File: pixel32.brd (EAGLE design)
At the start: 50 x 40 mm, 111 parts, among them CON1 DS1066-07M-SIDE, CON2 DS1066-07M-SIDE, CON3 PINHEAD_1X02-2.54, CON4 PINHEAD_1X01-2.54, CON5 PINHEAD_1X01-2.54, CON6 PINHEAD_1X01-2.54, CON7 PINHEAD_1X01-2.54, IC1 STM32F030K6TX-LQFP32(7X7), IC101 IRS44273L, IC201 IRS44273L, IC3 ST3485SOIC8, IC301 IRS44273L, IC6 MC74VHC1GT125, IC7 MC74VHC1GT125, IC8 LM317

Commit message: PCB Finalization #2
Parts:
- added FRAME1, FRAME101, FRAME201, FRAME301: RTU_A4, frames:A4L-LOC
- added FRAME2: RTU_A3, frames:A3L-LOC
- moved R10 4.16 mm to (-5.22, -1.82), turned to 45 degrees
- moved R13 3.03 mm to (-3.95, 0.70), turned to 180 degrees
- moved C18 2.73 mm to (-3.77, 2.02)
- moved SJ3 1.82 mm to (-15.7, -1.02)
- moved SJ1 1.81 mm to (-17.4, -1.02)
- moved R8 0.13 mm to (-5.92, 0.88)
- turned TP202 to 180 degrees
- turned TP101 to 270 degrees
- turned TP102 to 180 degrees
- turned TP104 to 180 degrees
- turned TP204 to 180 degrees
- turned TP301 to 270 degrees
- turned TP304 to 180 degrees
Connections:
- net LED1_CURRENT: now also IC1.12; no longer IC1.13
- net LED2_CURRENT: now also IC1.13; no longer IC1.12
- net LED3_CURRENT: now also IC1.14; no longer IC1.11
- net VIN_SENSE: now also IC1.11; no longer IC1.14
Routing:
- net VDD_24V: track 88.5 -> 82.1 mm, vias 81 -> 80
- net LED3_CURRENT: track 19.1 -> 12.8 mm
- net LED2_CURRENT: track 25.5 -> 23.0 mm, vias 2 -> 1
- net LED1_CURRENT: track 33.7 -> 31.3 mm
- net VIN_SENSE: track 7.12 -> 9.01 mm
- net GND: track 13.5 -> 11.8 mm, vias 121 -> 114
- net N$5: track 13.3 -> 12.2 mm
- net CLOCK: track 31.3 -> 30.2 mm
- net VDD_12V: track 35.9 -> 36.9 mm
- net LED2_PWM: track 13.9 -> 14.8 mm
- net CS_OUT: track 12.6 -> 12.0 mm
- net VDD_3V3: track 56.5 -> 57.0 mm

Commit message: blah
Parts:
- added PAD3: WIREPADSMD2.5-1.8, valenok_master_library:PAD-2.5-1.8
- added U$3: CONNECTION, usb2can_master_lib:CONNECTION
- R10: device rc:R0805 -> rc:R0603
- moved C24 2.31 mm to (12.7, 15.3), turned to 90 degrees
- moved RN2 2.10 mm to (13.4, 10.9)
- moved R10 1.93 mm to (-3.77, -0.55), turned to 0 degrees
- moved IC7 1.36 mm to (9.88, 15.1)
- moved C23 0.68 mm to (9.88, 12.8)
- moved R2 0.30 mm to (0.40, 3.70)
- moved IC6 0.19 mm to (9.88, 10.5)
- moved R13 0.18 mm to (-3.77, 0.70)
- moved C18 0.07 mm to (-3.77, 1.95)
- moved TP2 0.05 mm to (12.4, 14.3)
- moved R15 0.05 mm to (2.70, 4.08)
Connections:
- net CLOCK_BUFFERED: now also RN2.3; no longer RN2.2
- net GND: now also U$3.P$2
- net GNDD: now also U$3.P$1
- net N$15: now also RN2.6; no longer RN2.7
- net VDD_3V3: now also PAD3.P$1
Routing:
- net VDD_3V3: track 57.0 -> 61.6 mm
- net GND: track 11.8 -> 14.8 mm, vias 114 -> 102
- net VDD_24V: track 82.1 -> 84.2 mm
- net MOSI/DATA: track 34.8 -> 32.8 mm
- net RS485_B: track 40.8 -> 39.0 mm
- net RS485_A: track 43.0 -> 41.4 mm
- net N$19: track 2.80 -> 3.81 mm
- net A: track 10.9 -> 10.0 mm
- net N$14: track 3.55 -> 2.85 mm
- net VIN_SENSE: track 9.01 -> 9.68 mm
- net TX: track 2.42 -> 3.08 mm
- net CLOCK_BUFFERED: track 1.57 -> 2.20 mm
- net SWIO: track 9.76 -> 10.3 mm
- net VDD_12V: track 36.9 -> 37.5 mm
- net DATA_BUFFERED: track 4.29 -> 3.77 mm

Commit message: -pixel32 update
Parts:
- removed FRAME1, FRAME101, FRAME201, FRAME301: RTU_A4, frames:A4L-LOC
- removed FRAME2: RTU_A3, frames:A3L-LOC
- added CON10, CON11, CON8, CON9: PINHEAD_1X01-2.54, pinhead:1X01-PTH-2.54
- added CON12: PINHEAD_1X02-2.54, pinhead:1X02-PTH-2.54
- moved L102 0.25 mm to (20.8, -9.50)
- moved L202 0.25 mm to (12.2, -9.50)
- moved L302 0.25 mm to (3.75, -9.50)
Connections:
- net GND: now also CON12.2, CON3.2
- net N$10: now also CON9.1
- net N$21: now also CON10.1
- net N$23: now also CON11.1
- net TEMP: now also CON12.1; no longer R8.2
- net VDD_24V: now also CON8.1
- net VDD_3V3: now also R8.2; no longer CON3.2
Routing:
- net TEMP: track 10.1 -> 25.1 mm
- net N$10: track 0.00 -> 4.00 mm
- net VDD_24V: track 84.2 -> 88.1 mm
- net N$21: track 1.60 -> 5.35 mm
- net N$23: track 0.00 -> 3.00 mm
- net VDD_3V3: track 61.6 -> 59.2 mm, vias 10 -> 9
- net GNDD: track 49.2 -> 47.6 mm

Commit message: -pixel32 update
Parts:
- added D5: SMBJ26CA-SMB, ExitControl_v2_master_library:SMB
- U$1: value RTU -> (none)
- moved CON3 14.1 mm to (-7.47, -14.6)
- moved C26 2.14 mm to (-6.20, 0.05), turned to 180 degrees
- moved U$1 0.61 mm to (5.12, 9.25)
- moved R8 0.51 mm to (-6.20, 1.30), turned to 180 degrees
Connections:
- net GND: now also CON12.1, CON3.1, D5.A; no longer CON12.2, CON3.2, R8.1
- net TEMP: now also CON12.2, CON3.2, R8.1; no longer CON12.1, CON3.1
- net VDD_24V: now also D5.C
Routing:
- net VDD_3V3: track 59.2 -> 65.3 mm
- net TEMP: track 25.1 -> 30.5 mm, vias 0 -> 2
- net GND: vias 102 -> 111
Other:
- board text added: "TERM"
- board text removed: "12V"
- board text removed: "SUP"
- board text removed: "TERMINATOR"

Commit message: -more edge connectors
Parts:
- added CON13, CON14: PINHEAD_1X07-2, pinhead:1X07-PTH-2
- moved U$3 0.50 mm to (15.6, 12.0)
- moved U$6 0.50 mm to (15.6, 11.0)
- moved D1 0.20 mm to (-12.4, 11.6)
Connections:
- net GNDD: now also CON13.1, CON14.1
- net N$11: now also CON13.4
- net N$12: now also CON13.3
- net N$13: now also CON13.2
- net N$14: now also CON14.4
- net N$15: now also CON14.3
- net N$19: now also CON14.2
- net RS485_A: now also CON13.6, CON14.6
- net RS485_B: now also CON13.5, CON14.5
- net VDD_24V: now also CON13.7, CON14.7
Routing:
- net GNDD: track 47.6 -> 56.9 mm
- net RS485_B: track 39.0 -> 43.1 mm
- net RS485_A: track 41.4 -> 44.9 mm
- net VDD_24V: track 88.2 -> 91.6 mm
- net N$19: track 3.81 -> 5.80 mm
- net N$15: track 2.46 -> 4.45 mm
- net N$14: track 2.85 -> 4.84 mm
- net N$13: track 3.05 -> 5.04 mm
- net N$12: track 3.56 -> 5.55 mm
- net N$11: track 5.01 -> 7.00 mm
- net CLOCK: track 30.5 -> 29.4 mm
- net CS: track 21.2 -> 20.5 mm

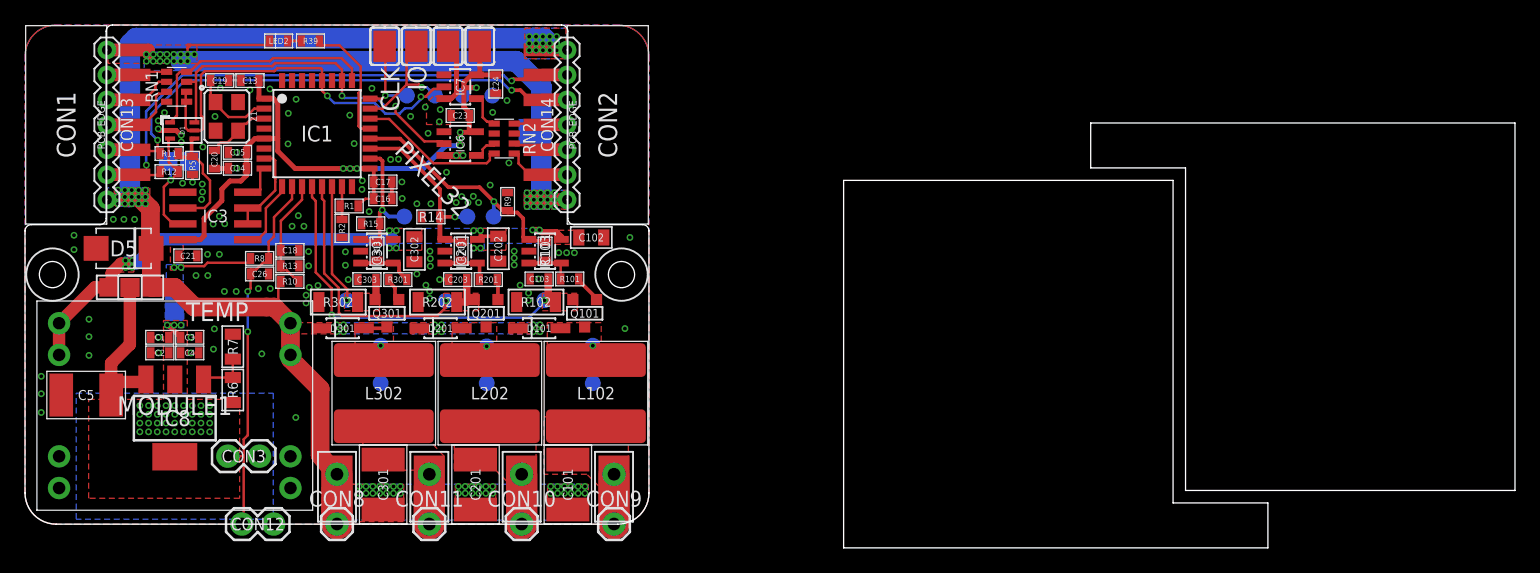
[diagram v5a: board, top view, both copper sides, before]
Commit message: voltage regulator recalculated, minor fixes, attributes
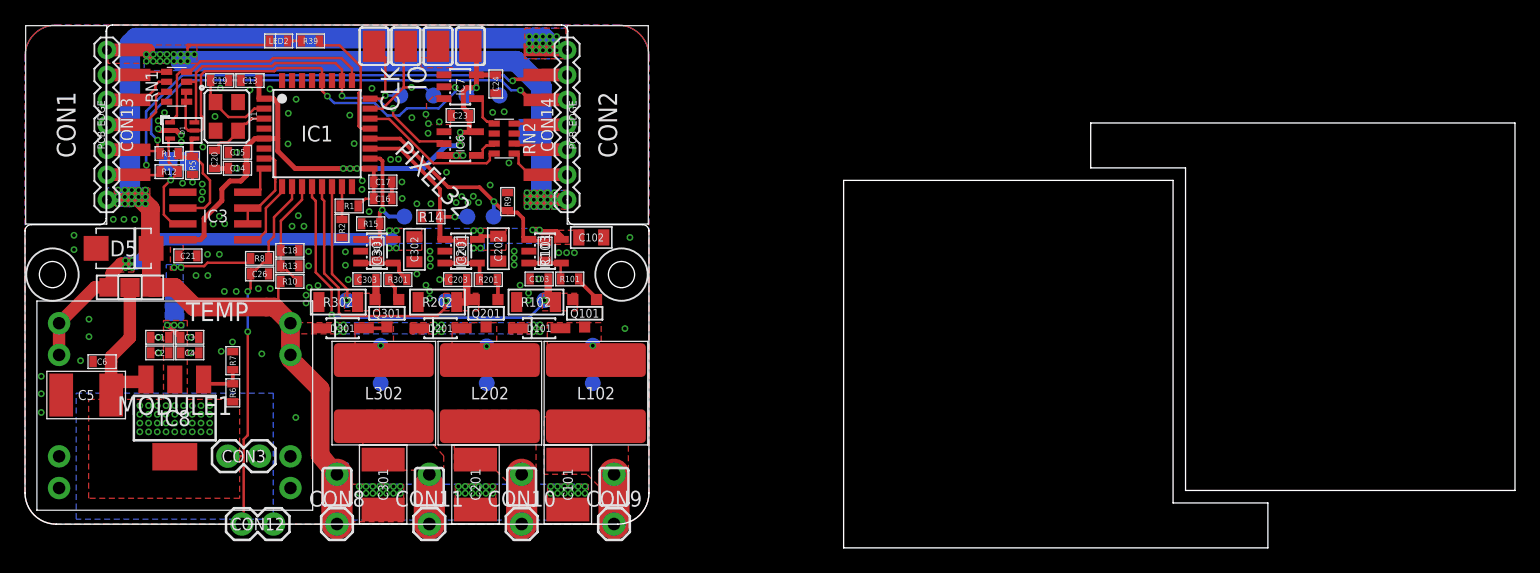
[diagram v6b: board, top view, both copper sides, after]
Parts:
- removed Z1: 16MHz, watchdog_master_library:OSCILLATOR-3.2X2.5
- added C6: 100 nF, rc:C0603
- added Y1: 16MHz, crystals:OSCILLATOR-3.2X2.5
- C19, C20: value (none) -> 10 pF
- C21: value 0.1uF -> 100 nF
- C5: value (none) -> 10 uF
- CON1, CON2: value DS1066-07M-SIDE -> B7B-PH-K-S-SIDE; device pixel_masterlib:DS1066-08M_SIDE -> pixel_masterlib:B7B-PH-K-S_SIDE
- D101, D201, D301: value CRS08-SOD123 -> DIODE-SOD123; device FMU_masterlib:SOD123 -> pixel_masterlib:SOD123
- D5: value SMBJ26CA-SMB -> TVS_DIODE-SMB; device ExitControl_v2_master_library:SMB -> pixel_masterlib:SMB
- IC8: device masterlib:SOT223 -> pixel_masterlib:SOT223
- LED_ANODE, LED_CATHODE1, LED_CATHODE2, LED_CATHODE3: value WIREPADSMD5-2,5 -> WIREPADSMD2.5-1.8; device valenok_master_library:5-2,5 -> wirepad:PAD-2.5-1.8
- MODULE1: device ali_modules:GW1584 -> pixel_masterlib:GW1584
- PAD1, PAD2, PAD3, PAD4: device valenok_master_library:PAD-2.5-1.8 -> wirepad:PAD-2.5-1.8
- R6: device rc:R0805 -> rc:R0603
- R7: value 5K6 -> 1K6; device rc:R0805 -> rc:R0603
- TP1, TP2, TP3, TP4: device pixhawk2:PAD.05X.05 -> misc:PAD.05X.05
- moved R7 1.12 mm to (-8.35, -6.90)
- moved PAD2 0.85 mm to (5.51, 18.3)
- moved PAD1 0.85 mm to (2.97, 18.3)
- moved PAD4 0.80 mm to (8.10, 18.3)
- moved PAD3 0.75 mm to (10.7, 18.3)
- moved TP2 0.58 mm to (13.0, 14.3)
- moved TP4 0.52 mm to (5.08, 14.3)
- moved TP3 0.30 mm to (10.4, 14.3)
- moved R6 0.22 mm to (-8.35, -9.47)
- moved TP1 0.12 mm to (7.72, 14.3)
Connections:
- net GND: now also C6.1, Y1.2, Y1.4; no longer Z1.2, Z1.4
- net N$10: now also LED_CATHODE1.P$1; no longer LED_CATHODE1.1
- net N$21: now also LED_CATHODE2.P$1; no longer LED_CATHODE2.1
- net N$23: now also LED_CATHODE3.P$1; no longer LED_CATHODE3.1
- net N$4: now also Y1.1; no longer Z1.1
- net N$5: now also C6.2
- net N$9: now also Y1.3; no longer Z1.3
- net VDD_24V: now also LED_ANODE.P$1; no longer LED_ANODE.1
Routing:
- net GND: track 14.6 -> 9.42 mm
- net MOSI/DATA: track 32.4 -> 34.7 mm
- net VDD_3V3: track 65.3 -> 63.9 mm
- net SWIO: track 10.3 -> 9.41 mm

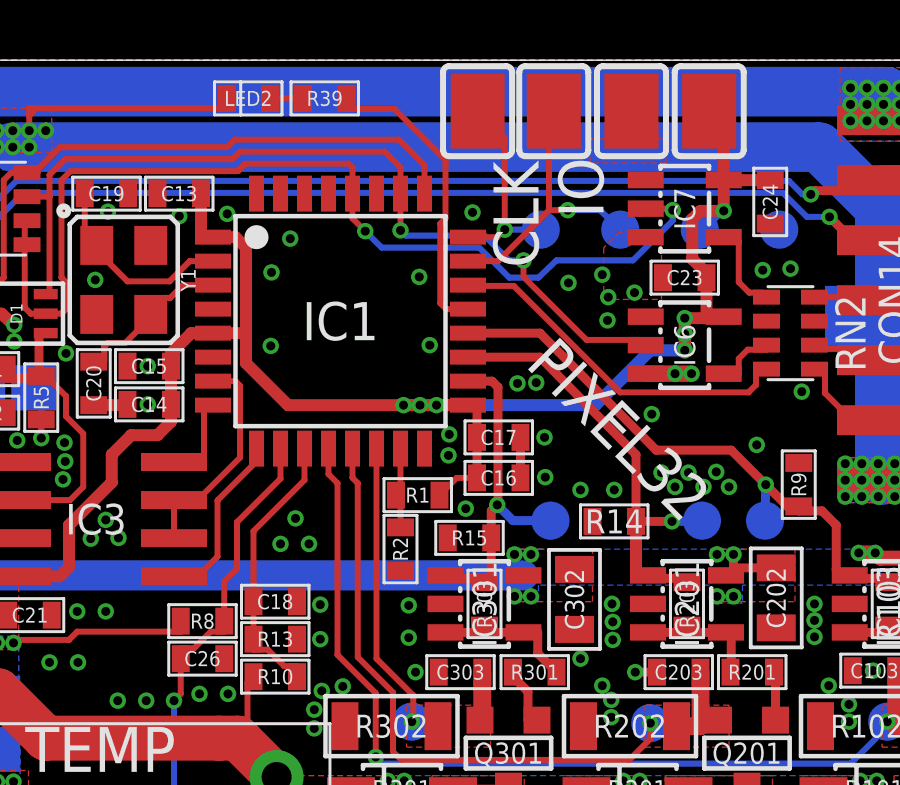
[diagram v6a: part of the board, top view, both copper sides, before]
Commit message: input sense divider values added boot0 fix
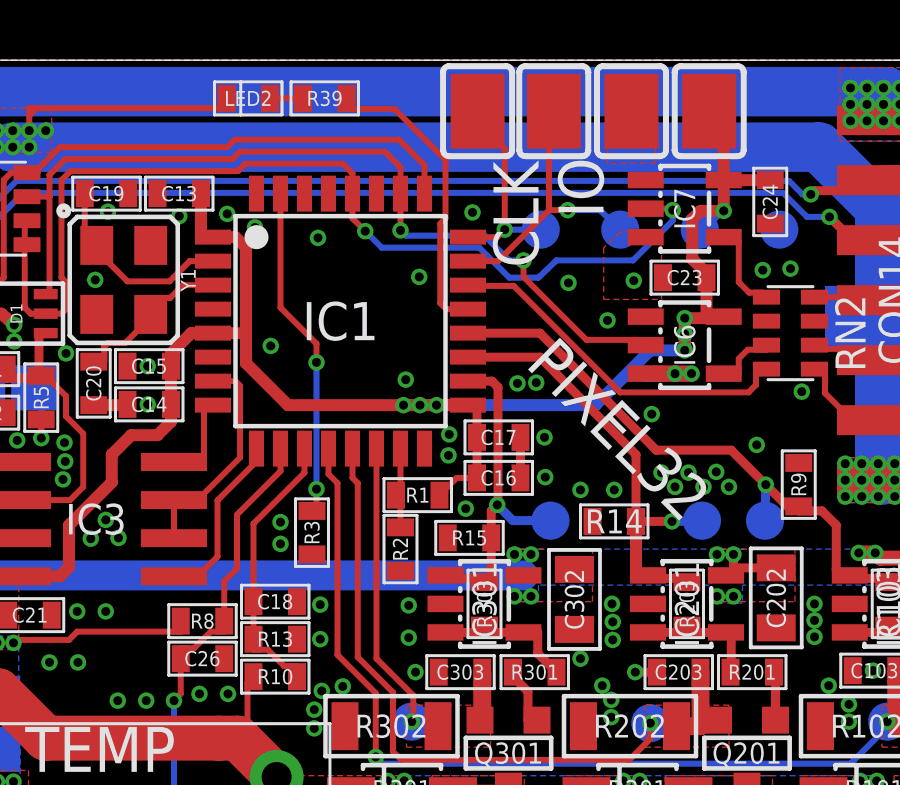
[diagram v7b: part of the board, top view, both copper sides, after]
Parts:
- added R3: 20K, rc:R0603
- R10: value (none) -> 100K
- R13: value (none) -> 10K
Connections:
- new net N$6: IC1.31, R3.1
- net GND: now also R3.2
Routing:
- net N$6: track 0.00 -> 11.2 mm, vias 0 -> 2
- net GND: vias 111 -> 108

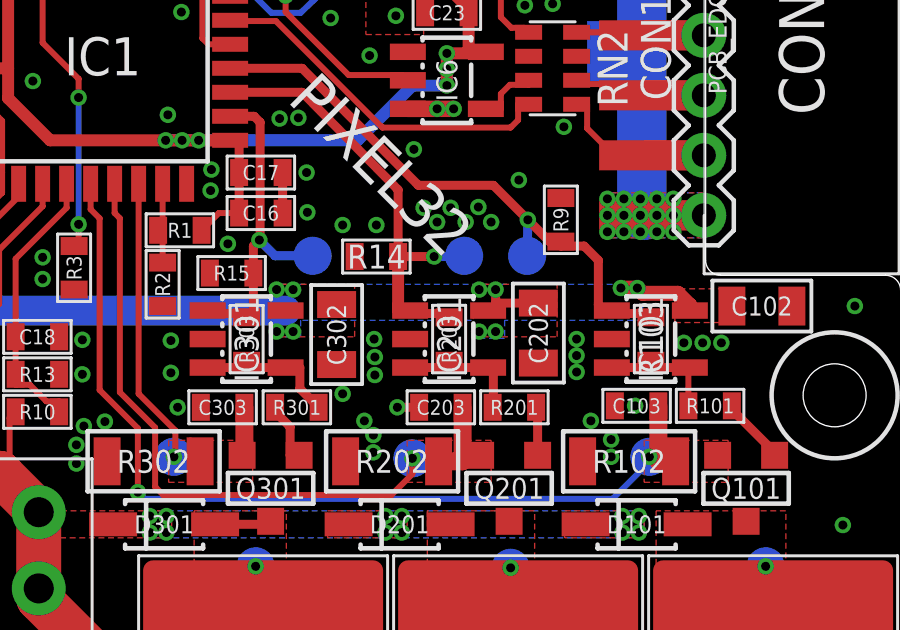
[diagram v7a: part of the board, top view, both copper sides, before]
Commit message: TME part numbers added
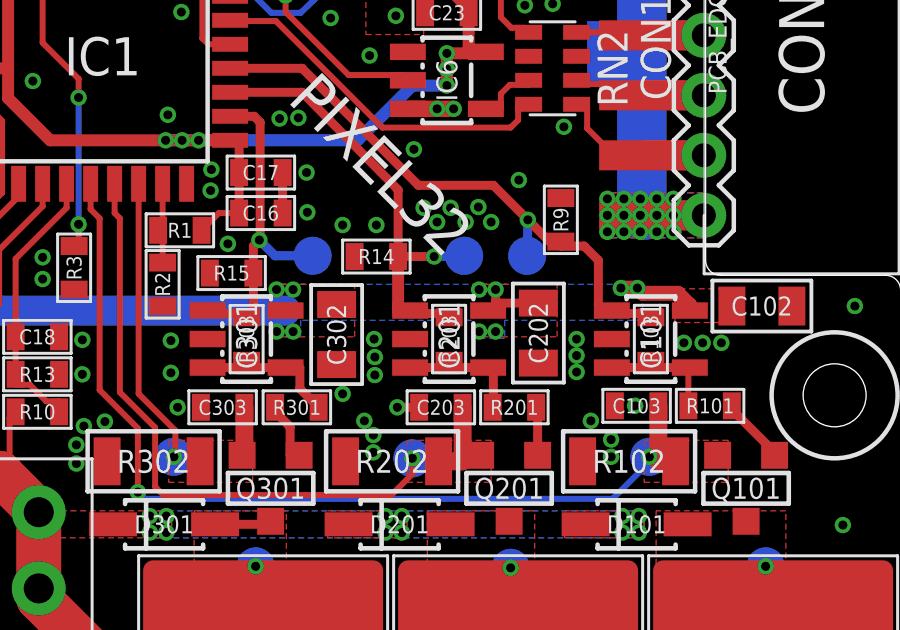
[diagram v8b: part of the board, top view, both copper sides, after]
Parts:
- R3: value 20K -> 10K
